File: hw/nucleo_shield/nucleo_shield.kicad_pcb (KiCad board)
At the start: 2 copper layers, 151 x 90.9 mm, 75 parts, among them CN101 Nucleo-F411RE-CN10, CN71 Nucleo-F411RE-CN7, P1 CONN_INH1, P10 CONN_OUTH1, P11 CONN_OUTH2, P12 CONN_RS485_OUT, P13 CONN_RS485_IN, P14 CONN_OUT2, P15 CONN_EXT2, P16 CONN_EXTI2C, P17 CONN_EXT, P18 CONN_1WIRE, P19 CONN_EXT_SPI, P2 CONN_OUT3, P3 CONN_OUT1, P4 POWER_CON, P5 CONN_INH2, P6 ETH_CONN, P7 CONN_LCD_SD, P8 CONN_OUT4, P9 CONN_SCT, U1 74HC595, U10 ULN2803, U11 74HC595, U12 74HC595, U2 74HC595, U3 LTV-847, U4 LTV-847, U5 LTV-847, U6 LTV-847, U7 PCF8574A, U8 PCF8574A, U9 ULN2803

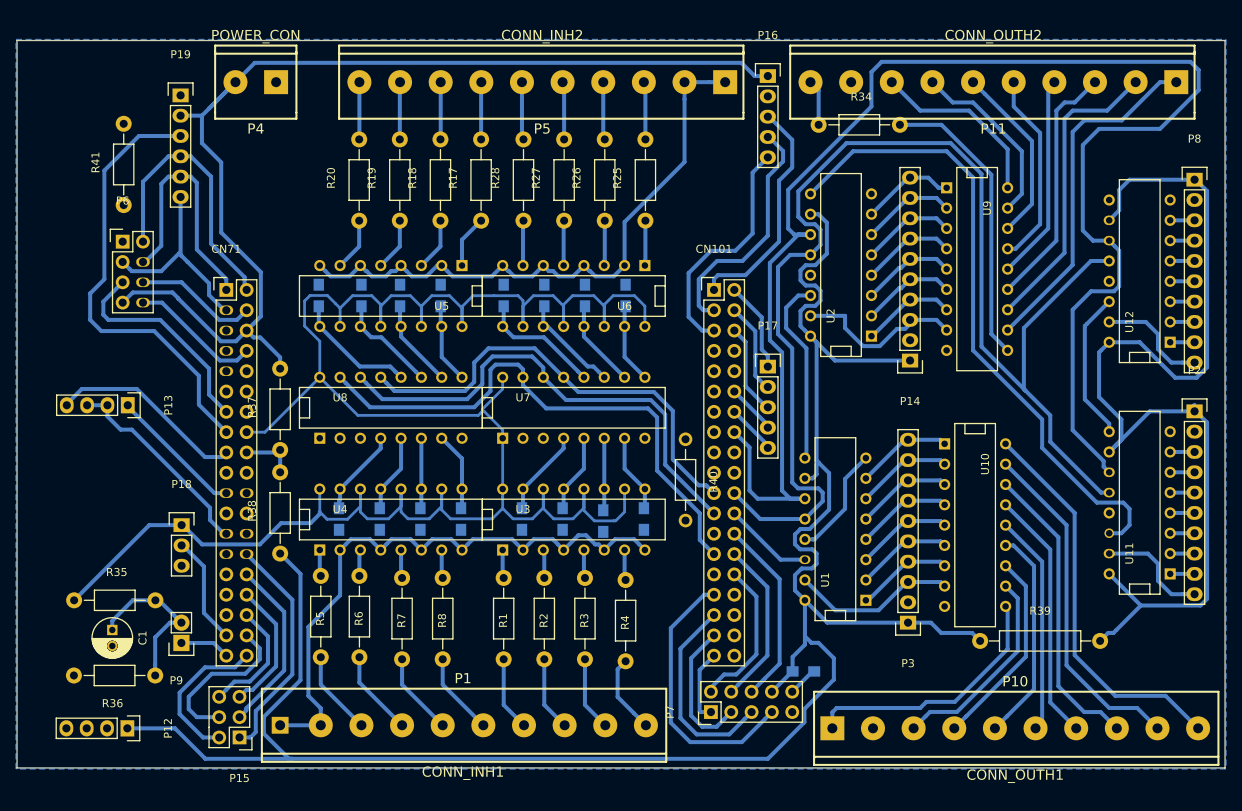
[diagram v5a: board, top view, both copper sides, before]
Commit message: Nucleo: Add mounting holes, add more spacing between tracks
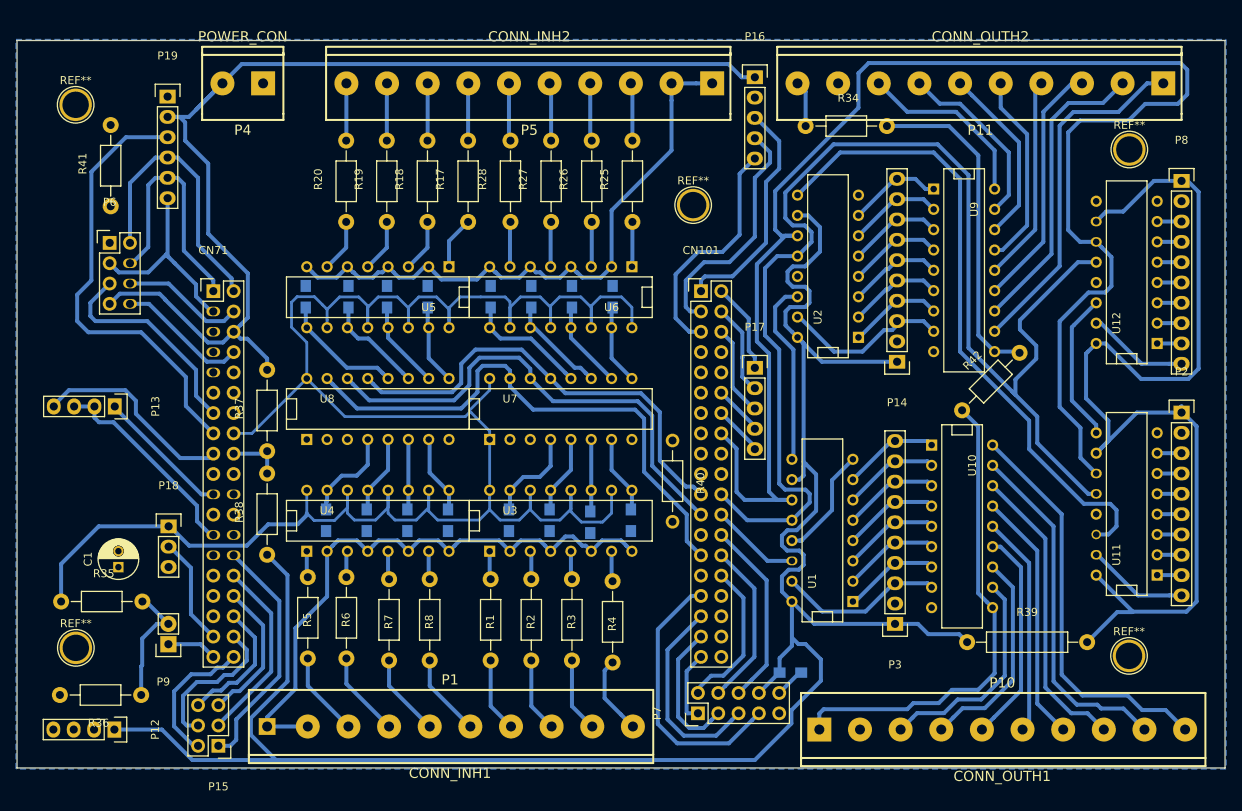
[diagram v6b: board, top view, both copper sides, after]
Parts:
- added R42: R, Resistors_ThroughHole:Resistor_Horizontal_RM10mm, F.Cu at (213.3, 104.3)
- added REF**: 1pin, Connect:1pin, F.Cu at (179.6, 78.6)
- added REF**: 1pin, Connect:1pin, F.Cu at (234.2, 71.7)
- added REF**: 1pin, Connect:1pin, F.Cu at (102.5, 134.0)
- added REF**: 1pin, Connect:1pin, F.Cu at (234.1, 135.0)
- added REF**: 1pin, Connect:1pin, F.Cu at (102.5, 66.1)
- moved C1 7.89 mm to (107.8, 123.9), turned to 90 degrees
- moved R36 3.00 mm to (110.6, 139.9)
- moved P15 2.84 mm to (120.3, 146.2)
- moved P3 1.63 mm to (204.9, 131.0)
- moved P5 1.63 mm to (159.2, 63.4)
- moved R10 1.63 mm to (149.0, 118.0)
- moved R11 1.63 mm to (131.2, 90.1)
- moved R21 1.63 mm to (141.4, 90.1)
- moved R25 1.63 mm to (172.0, 80.7)
- moved R3 1.63 mm to (164.5, 130.5)
- moved R31 1.63 mm to (164.5, 90.1)
- moved R34 1.63 mm to (198.8, 68.7)
- moved R8 1.63 mm to (146.7, 130.5)
- moved U1 1.63 mm to (195.8, 119.3)
- moved U4 1.63 mm to (140.2, 118.1)
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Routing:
- net +24V: track 39.1 -> 67.0 mm
- net Net-(C1-Pad1): track 20.8 -> 15.6 mm
- net +5V: track 524.0 -> 529.2 mm
- net Net-(R34-Pad2): track 36.8 -> 41.5 mm
- net SRLatch: track 157.5 -> 160.3 mm
- net +3V3: track 263.6 -> 266.3 mm
- net SRCLK: track 193.0 -> 195.1 mm
- net out1h: track 25.8 -> 27.5 mm
- net out2h: track 25.1 -> 26.7 mm
- net Net-(CN71-Pad38): track 19.1 -> 17.6 mm
- net Net-(CN71-Pad36): track 20.3 -> 18.8 mm
- net Net-(CN71-Pad28): track 28.8 -> 30.2 mm
- net Net-(CN71-Pad32): track 16.6 -> 18.0 mm
- net Net-(CN71-Pad34): track 15.0 -> 16.4 mm
- net out8h: track 49.2 -> 50.6 mm
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
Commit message: Nucleo: Add marking
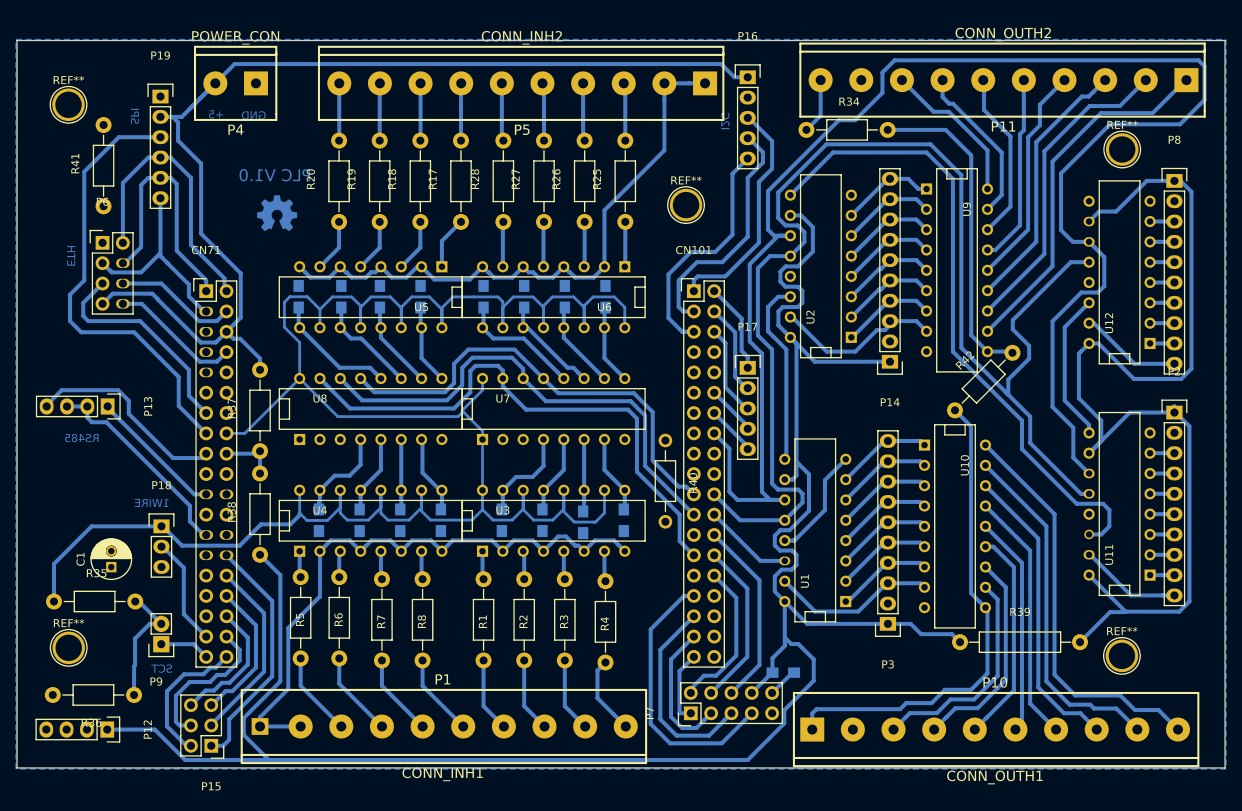
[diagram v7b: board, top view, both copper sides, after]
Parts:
- added G***: LOGO, LOGO, B.Cu at (127.6, 79.6)
- moved P11 2.92 mm to (218.4, 63.0)
- moved CN101 0.89 mm to (179.7, 89.4)
- moved CN71 0.89 mm to (118.8, 89.4)
- moved P1 0.89 mm to (148.4, 143.8)
- moved P10 0.89 mm to (217.4, 144.2)
- moved P14 0.89 mm to (204.2, 98.2)
- moved P16 0.89 mm to (186.5, 62.6)
- moved P17 0.89 mm to (186.5, 99.0)
- moved P2 0.89 mm to (239.8, 104.5)
- moved P7 0.89 mm to (179.3, 142.1)
- moved P8 0.89 mm to (239.8, 75.6)
- moved P9 0.89 mm to (113.2, 133.5)
- moved R1 0.89 mm to (153.4, 130.5)
- moved R13 0.89 mm to (143.0, 118.0)
- moved R14 0.89 mm to (135.7, 90.1)
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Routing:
- net out16h: track 22.8 -> 19.2 mm
- net SRCLK: track 195.1 -> 198.1 mm
- net out15h: track 22.6 -> 20.2 mm
- net out12h: track 25.8 -> 27.8 mm
- net out11h: track 31.2 -> 32.9 mm
- net out10h: track 37.6 -> 39.3 mm
- net out9h: track 44.2 -> 45.5 mm
- net out14h: track 22.6 -> 21.3 mm
- net Net-(R34-Pad2): track 41.5 -> 40.3 mm
- net out13h: track 24.5 -> 23.7 mm
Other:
- board text added: "+5"
- board text added: "1WIRE"
- board text added: "ETH"
- board text added: "GND"
- board text added: "I2C"
- board text added: "PLC V1.0"
- board text added: "RS485"
- board text added: "SCT"
- board text added: "SPI"

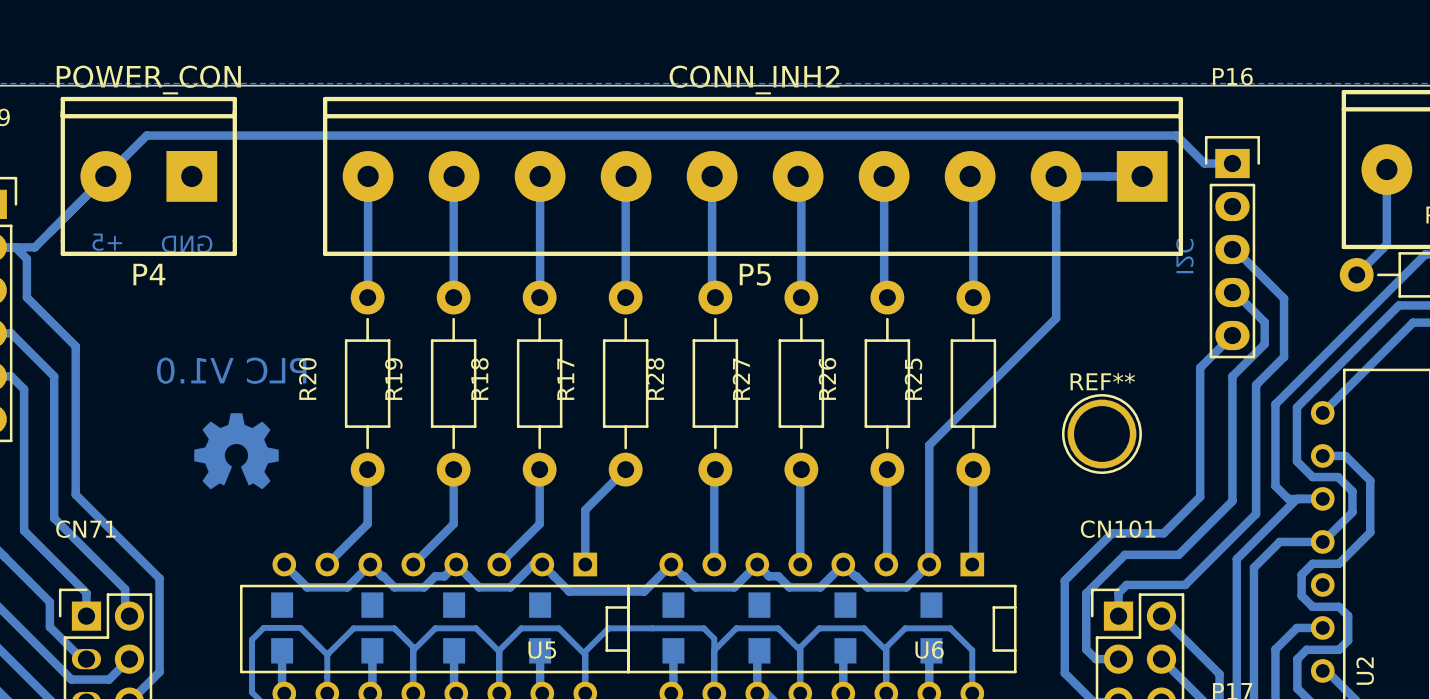
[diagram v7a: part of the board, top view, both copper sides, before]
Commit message: Nucleo: add BME180 header on PCB
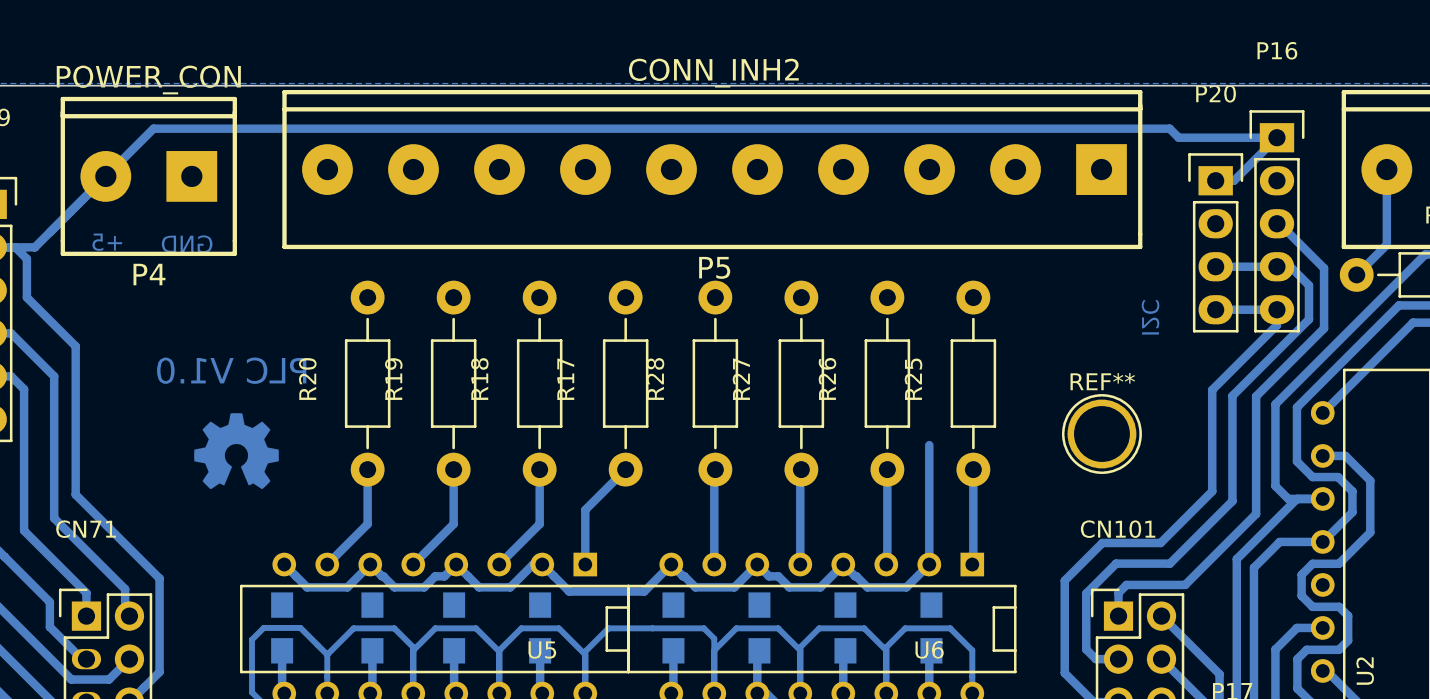
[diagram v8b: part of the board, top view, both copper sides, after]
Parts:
- added P20: CON_BME, Pin_Headers:Pin_Header_Straight_1x04, F.Cu at (185.5, 63.7)
- moved P16 3.04 mm to (189.1, 61.1)
- moved P5 2.43 mm to (155.9, 63.0)
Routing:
- net GND_24V: track 153.7 -> 129.6 mm
- net inh16: track 7.24 -> 0.00 mm
- net inh14: track 7.24 -> 0.00 mm
- net inh11: track 7.17 -> 0.00 mm
- net inh10: track 7.17 -> 0.00 mm
- net inh9: track 7.17 -> 0.04 mm
- net inh12: track 7.17 -> 0.04 mm
- net +5V: track 529.2 -> 536.2 mm
- net inh15: track 7.24 -> 0.27 mm
- net inh13: track 7.24 -> 0.27 mm
- net I2C1_SCL: track 30.7 -> 37.3 mm
- net I2C1_SDA: track 29.7 -> 36.2 mm
- net I2C_GPIO: track 29.1 -> 31.5 mm
